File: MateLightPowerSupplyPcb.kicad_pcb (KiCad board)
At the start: 2 copper layers, 73 x 26 mm, 28 parts, among them X1 Power IN, X10 JST ZE 2, X11 JST ZE 2, X12 JST ZE 2, X13 JST ZE 2, X14 JST ZE 2, X15 JST ZE 2, X16 JST ZE 2, X17 JST ZE 2, X18 JST ZE 2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

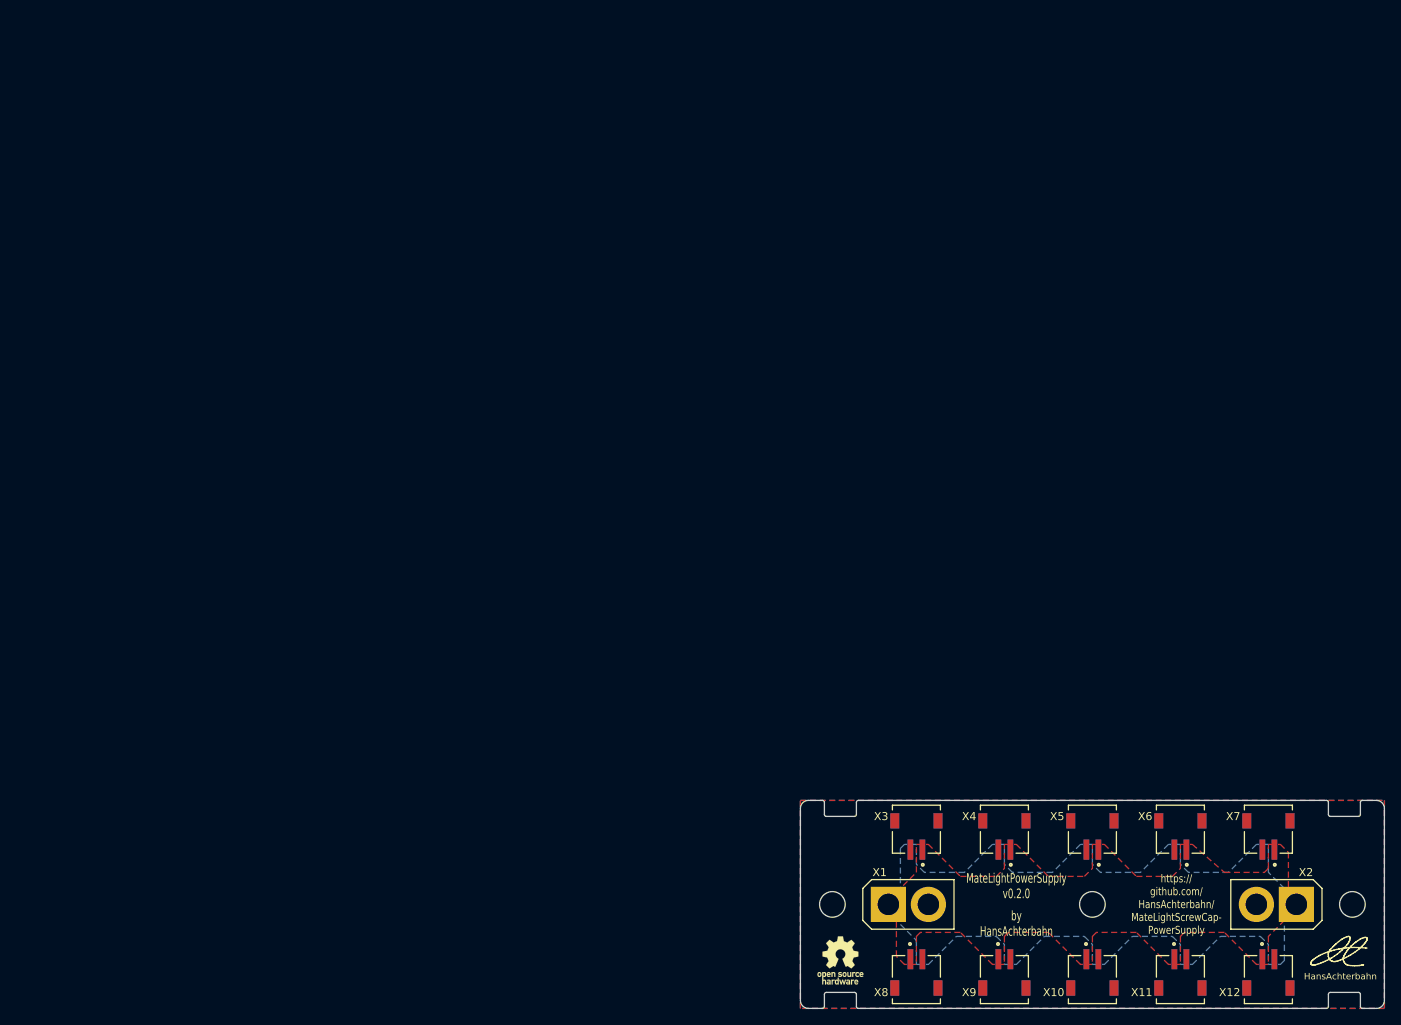
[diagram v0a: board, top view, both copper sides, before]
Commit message: Changed board page to simply just fit the pcb
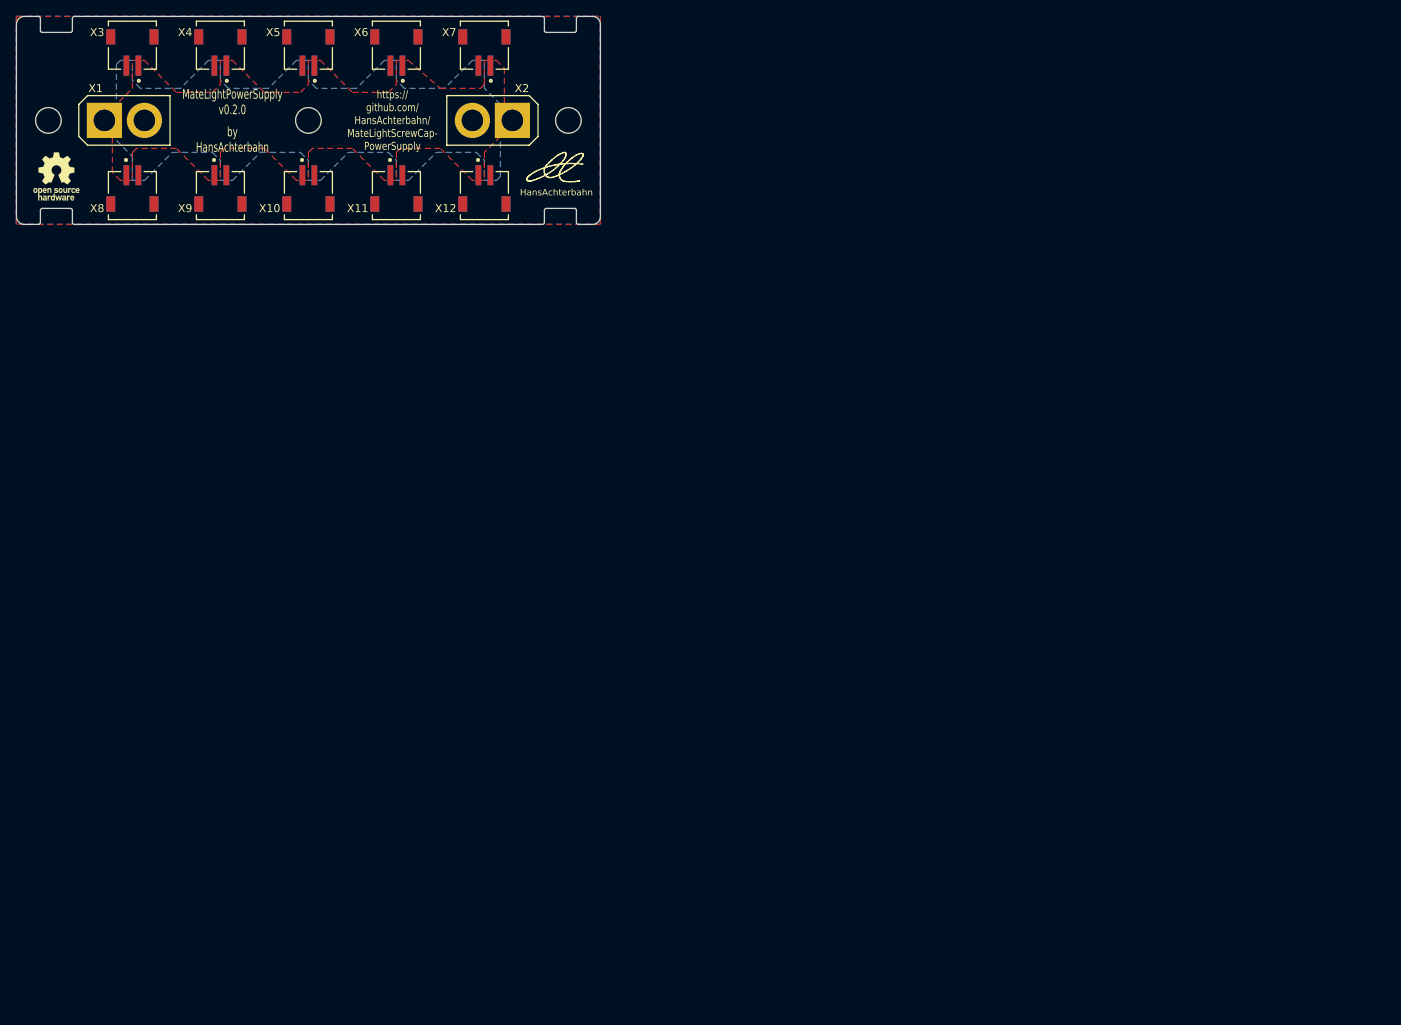
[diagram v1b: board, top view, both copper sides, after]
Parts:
- moved H1 138.6 mm to (6.00, 15.0)
- moved H2 138.6 mm to (38.5, 15.0)
- moved H3 138.6 mm to (71.0, 15.0)
- moved REF** 138.6 mm to (70.0, 21.0)
- moved REF** 138.6 mm to (7.00, 22.0)
- moved REF** 138.6 mm to (49.0, 15.0)
- moved X1 138.6 mm to (15.5, 15.0)
- moved X10 138.6 mm to (38.5, 24.0)
- moved X11 138.6 mm to (49.5, 24.0)
- moved X12 138.6 mm to (60.5, 24.0)
- moved X13 138.6 mm to (60.5, 6.00)
- moved X14 138.6 mm to (49.5, 6.00)
- moved X15 138.6 mm to (38.5, 6.00)
- moved X16 138.6 mm to (27.5, 6.00)
- moved X17 138.6 mm to (16.5, 6.00)
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
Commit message: sync: schematic → board
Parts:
- removed REF**: h8-Logo-4mm, h8-Logos:h8-Logo-4mm
- removed REF**: OSHW-Logo_5.7x6mm_SilkScreen, Symbol:OSHW-Logo_5.7x6mm_SilkScreen
- removed REF**: KiCad-Logo2_5mm_SilkScreen, Symbol:KiCad-Logo2_5mm_SilkScreen
